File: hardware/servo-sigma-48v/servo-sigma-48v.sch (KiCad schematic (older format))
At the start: 0 parts

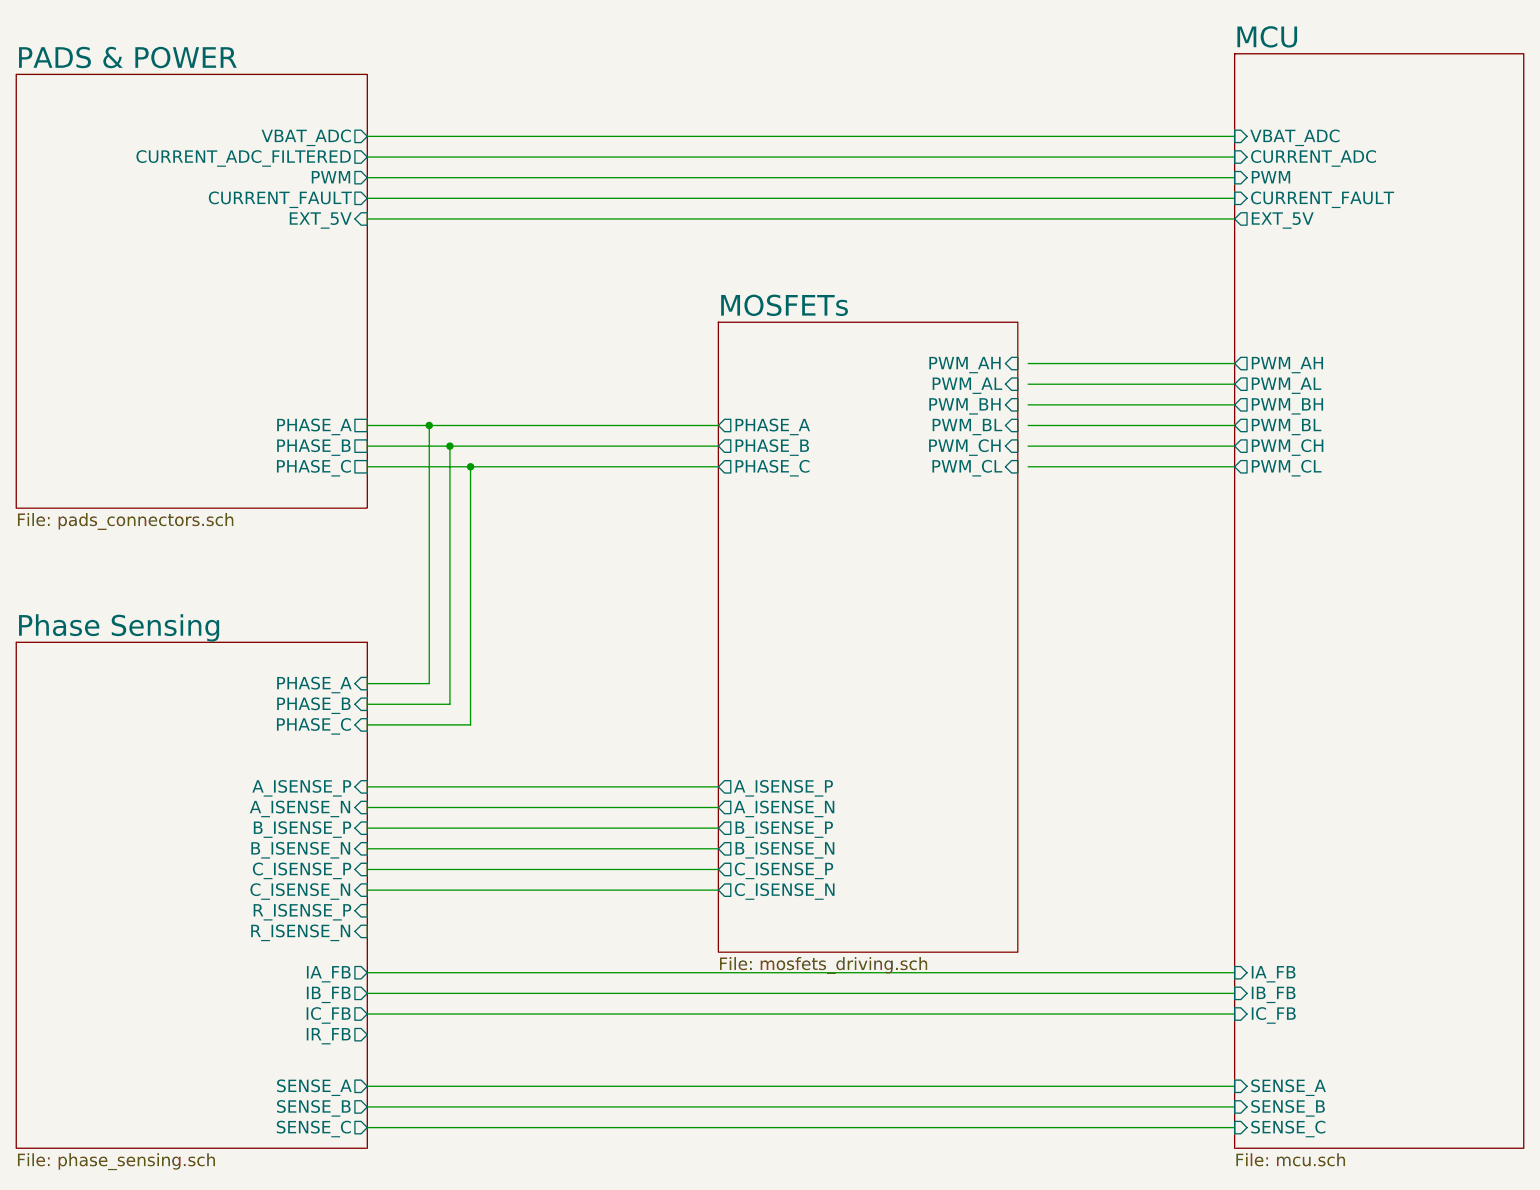
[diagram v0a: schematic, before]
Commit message: Finished routing of the servo controller
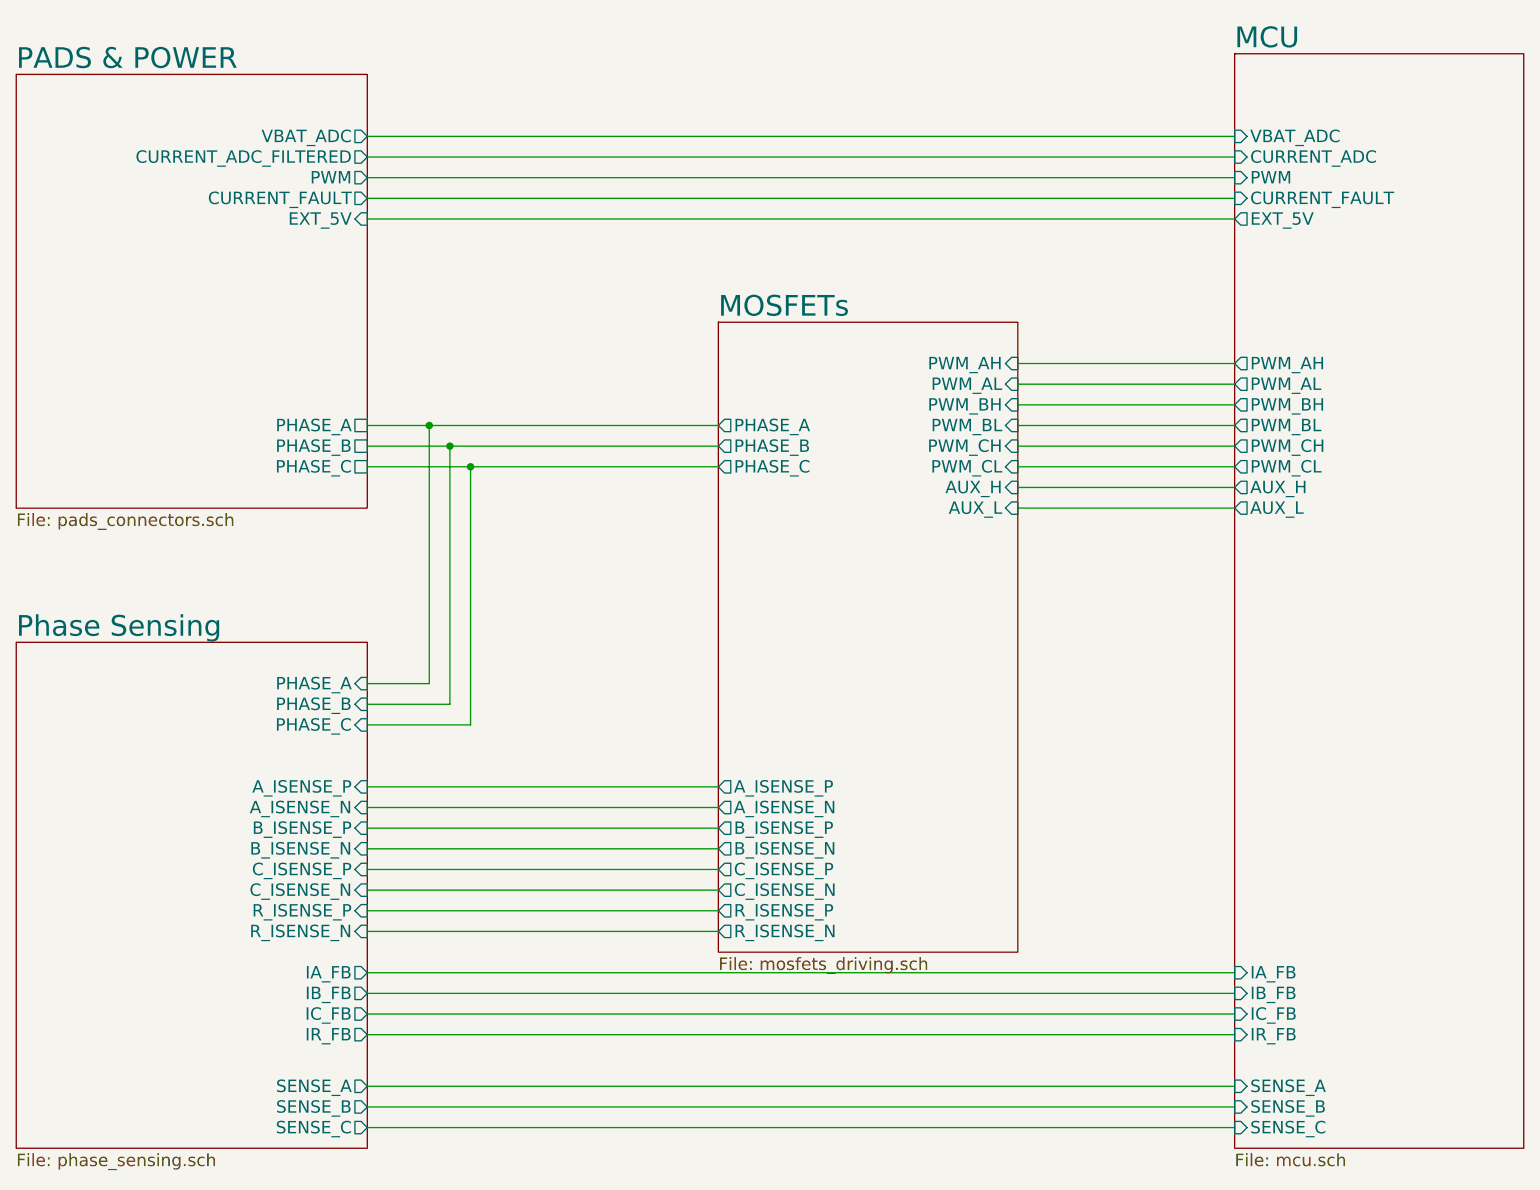
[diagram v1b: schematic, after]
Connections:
- wire segments 35 -> 40
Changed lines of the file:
@@
 F15 "C_ISENSE_P" O L 5200 4750 60
 F16 "C_ISENSE_N" O L 5200 4850 60
+F17 "AUX_L" I R 6650 3000 60
+F18 "AUX_H" I R 6650 2900 60
+F19 "R_ISENSE_P" O L 5200 4950 60
+F20 "R_ISENSE_N" O L 5200 5050 60
 $EndSheet
 $Sheet
@@
 F17 "IB_FB" I L 7700 5350 60
 F18 "IC_FB" I L 7700 5450 60
+F19 "AUX_L" O L 7700 3000 60
+F20 "AUX_H" O L 7700 2900 60
+F21 "IR_FB" I L 7700 5550 60
 $EndSheet
 Wire Wire Line
@@
 	3500 6000 7700 6000
 Wire Wire Line
-	6700 2300 7700 2300
+	6650 2300 7700 2300
 Wire Wire Line
-	6700 2400 7700 2400
+	6650 2400 7700 2400
 Wire Wire Line
-	6700 2500 7700 2500
+	6650 2500 7700 2500
 Wire Wire Line
-	6700 2600 7700 2600
+	6650 2600 7700 2600
 Wire Wire Line
-	6700 2700 7700 2700
+	6650 2700 7700 2700
 Wire Wire Line
-	6700 2800 7700 2800
+	6650 2800 7700 2800
 Wire Wire Line
 	3500 5250 7700 5250
@@
 Wire Wire Line
 	3500 5450 7700 5450
+Wire Wire Line
+	6650 2900 7700 2900
+Wire Wire Line
+	6650 3000 7700 3000
+Wire Wire Line
+	3500 4950 5200 4950
+Wire Wire Line
+	3500 5050 5200 5050
+Wire Wire Line
+	3500 5550 7700 5550
 $EndSCHEMATC

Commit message: Work on sigmadrive 2.0
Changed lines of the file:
@@
 F3 "PHASE_B" U R 3500 2700 60
 F4 "PHASE_C" U R 3500 2800 60
-F5 "CURRENT_ADC_FILTERED" O R 3500 1300 60
-F6 "CURRENT_FAULT" O R 3500 1500 60
-F7 "VBAT_ADC" O R 3500 1200 60
-F8 "PWM" O R 3500 1400 60
-F9 "EXT_5V" I R 3500 1600 60
+F5 "VBAT_ADC" O R 3500 1200 60
+F6 "PWM" O R 3500 1400 60
+F7 "EXT_5V" I R 3500 1600 60
 $EndSheet
 Wire Wire Line
@@
 Wire Wire Line
 	3500 1200 7700 1200
-Wire Wire Line
-	3500 1300 7700 1300
 Wire Wire Line
 	3500 1400 7700 1400
@@
 Connection ~ 4000 2800
 Wire Wire Line
-	3500 1500 7700 1500
-Wire Wire Line
 	3800 2600 5200 2600
 Wire Wire Line
@@
 F4 "SENSE_B" I L 7700 5900 60
 F5 "SENSE_C" I L 7700 6000 60
-F6 "CURRENT_ADC" I L 7700 1300 60
-F7 "PWM_AH" O L 7700 2300 60
-F8 "PWM_AL" O L 7700 2400 60
-F9 "PWM_BH" O L 7700 2500 60
-F10 "PWM_BL" O L 7700 2600 60
-F11 "PWM_CH" O L 7700 2700 60
-F12 "PWM_CL" O L 7700 2800 60
-F13 "PWM" I L 7700 1400 60
-F14 "CURRENT_FAULT" I L 7700 1500 60
-F15 "EXT_5V" O L 7700 1600 60
-F16 "IA_FB" I L 7700 5250 60
-F17 "IB_FB" I L 7700 5350 60
-F18 "IC_FB" I L 7700 5450 60
-F19 "AUX_L" O L 7700 3000 60
-F20 "AUX_H" O L 7700 2900 60
-F21 "IR_FB" I L 7700 5550 60
+F6 "PWM_AH" O L 7700 2300 60
+F7 "PWM_AL" O L 7700 2400 60
+F8 "PWM_BH" O L 7700 2500 60
+F9 "PWM_BL" O L 7700 2600 60
+F10 "PWM_CH" O L 7700 2700 60
+F11 "PWM_CL" O L 7700 2800 60
+F12 "PWM" I L 7700 1400 60
+F13 "EXT_5V" O L 7700 1600 60
+F14 "IA_FB" I L 7700 5250 60
+F15 "IB_FB" I L 7700 5350 60
+F16 "IC_FB" I L 7700 5450 60
+F17 "AUX_L" O L 7700 3000 60
+F18 "AUX_H" O L 7700 2900 60
+F19 "IR_FB" I L 7700 5550 60
 $EndSheet
 Wire Wire Line

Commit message: completed routing
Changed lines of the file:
@@
 $Descr A4 11693 8268
 encoding utf-8
-Sheet 1 5
+Sheet 1 4
 Title "Servo Driver 48V"
 Date "2018-09-03"
@@
 F6 "SENSE_B" O R 3500 5900 60
 F7 "SENSE_A" O R 3500 5800 60
-F8 "A_ISENSE_P" I R 3500 4350 60
-F9 "A_ISENSE_N" I R 3500 4450 60
-F10 "IA_FB" O R 3500 5250 60
-F11 "B_ISENSE_P" I R 3500 4550 60
-F12 "B_ISENSE_N" I R 3500 4650 60
-F13 "IB_FB" O R 3500 5350 60
-F14 "C_ISENSE_P" I R 3500 4750 60
-F15 "C_ISENSE_N" I R 3500 4850 60
-F16 "IC_FB" O R 3500 5450 60
-F17 "IR_FB" O R 3500 5550 60
-F18 "R_ISENSE_P" I R 3500 4950 60
-F19 "R_ISENSE_N" I R 3500 5050 60
 $EndSheet
 $Sheet
@@
 F2 "PWM_AH" I R 6650 2300 60
 F3 "PWM_AL" I R 6650 2400 60
-F4 "PHASE_A" O L 5200 2600 60
+F4 "PHASE_A" O L 5200 3850 60
 F5 "PWM_BH" I R 6650 2500 60
 F6 "PWM_BL" I R 6650 2600 60
-F7 "PHASE_B" O L 5200 2700 60
+F7 "PHASE_B" O L 5200 3950 60
 F8 "PWM_CH" I R 6650 2700 60
 F9 "PWM_CL" I R 6650 2800 60
-F10 "PHASE_C" O L 5200 2800 60
-F11 "A_ISENSE_P" O L 5200 4350 60
-F12 "A_ISENSE_N" O L 5200 4450 60
-F13 "B_ISENSE_P" O L 5200 4550 60
-F14 "B_ISENSE_N" O L 5200 4650 60
-F15 "C_ISENSE_P" O L 5200 4750 60
-F16 "C_ISENSE_N" O L 5200 4850 60
-F17 "AUX_L" I R 6650 3000 60
-F18 "AUX_H" I R 6650 2900 60
-F19 "R_ISENSE_P" O L 5200 4950 60
-F20 "R_ISENSE_N" O L 5200 5050 60
+F10 "PHASE_C" O L 5200 4050 60
+F11 "GATE_ENABLE" I R 6650 3200 60
+F12 "DRV_SDI" I R 6650 3300 60
+F13 "DRV_SDO" O R 6650 3400 60
+F14 "DRV_CLK" I R 6650 3500 60
+F15 "DRV1_CS" I R 6650 3600 60
+F16 "DRV_CAL" I R 6650 3800 60
+F17 "DRV_FAULT" O R 6650 3900 60
+F18 "DRV_SOC" O R 6650 4100 60
+F19 "DRV_SOB" O R 6650 4200 60
+F20 "DRV_SOA" O R 6650 4300 60
+F21 "EXT_5V" I R 6650 4550 60
+F22 "VBAT_ADC" O R 6650 4450 60
+F23 "DRV2_CS" I R 6650 3700 60
+F24 "PWM_RH" I R 6650 2900 60
+F25 "PWM_RL" I R 6650 3000 60
 $EndSheet
-$Sheet
-S 1800 900  1700 2100
-U 58BE27E6
-F0 "PADS & POWER" 100
-F1 "pads_connectors.sch" 60
-F2 "PHASE_A" U R 3500 2600 60
-F3 "PHASE_B" U R 3500 2700 60
-F4 "PHASE_C" U R 3500 2800 60
-F5 "VBAT_ADC" O R 3500 1200 60
-F6 "PWM" O R 3500 1400 60
-F7 "EXT_5V" I R 3500 1600 60
-$EndSheet
-Wire Wire Line
-	3500 2600 3800 2600
-Wire Wire Line
-	3500 2700 3900 2700
-Wire Wire Line
-	3500 2800 4000 2800
-Wire Wire Line
-	3500 1200 7700 1200
-Wire Wire Line
-	3500 1400 7700 1400
-Wire Wire Line
-	3500 3850 3800 3850
-Wire Wire Line
-	3800 3850 3800 2600
-Connection ~ 3800 2600
-Wire Wire Line
-	3500 3950 3900 3950
-Wire Wire Line
-	3900 3950 3900 2700
-Connection ~ 3900 2700
-Wire Wire Line
-	3500 4050 4000 4050
-Wire Wire Line
-	4000 4050 4000 2800
-Connection ~ 4000 2800
-Wire Wire Line
-	3800 2600 5200 2600
-Wire Wire Line
-	3900 2700 5200 2700
-Wire Wire Line
-	4000 2800 5200 2800
 $Sheet
 S 7700 800  1400 5300
@@
 F0 "MCU" 100
 F1 "mcu.sch" 60
-F2 "VBAT_ADC" I L 7700 1200 60
-F3 "SENSE_A" I L 7700 5800 60
-F4 "SENSE_B" I L 7700 5900 60
-F5 "SENSE_C" I L 7700 6000 60
-F6 "PWM_AH" O L 7700 2300 60
-F7 "PWM_AL" O L 7700 2400 60
-F8 "PWM_BH" O L 7700 2500 60
-F9 "PWM_BL" O L 7700 2600 60
-F10 "PWM_CH" O L 7700 2700 60
-F11 "PWM_CL" O L 7700 2800 60
-F12 "PWM" I L 7700 1400 60
-F13 "EXT_5V" O L 7700 1600 60
-F14 "IA_FB" I L 7700 5250 60
-F15 "IB_FB" I L 7700 5350 60
-F16 "IC_FB" I L 7700 5450 60
-F17 "AUX_L" O L 7700 3000 60
-F18 "AUX_H" O L 7700 2900 60
-F19 "IR_FB" I L 7700 5550 60
+F2 "SENSE_A" I L 7700 5800 60
+F3 "SENSE_B" I L 7700 5900 60
+F4 "SENSE_C" I L 7700 6000 60
+F5 "PWM_AH" O L 7700 2300 60
+F6 "PWM_AL" O L 7700 2400 60
+F7 "PWM_BH" O L 7700 2500 60
+F8 "PWM_BL" O L 7700 2600 60
+F9 "PWM_CH" O L 7700 2700 60
+F10 "PWM_CL" O L 7700 2800 60
+F11 "IA_FB" I L 7700 4300 60
+F12 "IB_FB" I L 7700 4200 60
+F13 "IC_FB" I L 7700 4100 60
+F14 "AUX_L" O L 7700 3000 60
+F15 "AUX_H" O L 7700 2900 60
+F16 "EXT_5V" O L 7700 4550 60
+F17 "VBAT_ADC" I L 7700 4450 60
+F18 "DRV_SDI" O L 7700 3300 60
+F19 "DRV_SDO" I L 7700 3400 60
+F20 "DRV_CLK" O L 7700 3500 60
+F21 "DRV1_CS" O L 7700 3600 60
+F22 "DRV_CAL" O L 7700 3800 60
+F23 "DRV_FAULT" I L 7700 3900 60
+F24 "GATE_ENABLE" O L 7700 3200 60
+F25 "DRV2_CS" O L 7700 3700 60
 $EndSheet
-Wire Wire Line
-	3500 1600 7700 1600
-Wire Wire Line
-	3500 4350 5200 4350
-Wire Wire Line
-	3500 4450 5200 4450
-Wire Wire Line
-	3500 4550 5200 4550
-Wire Wire Line
-	3500 4650 5200 4650
-Wire Wire Line
-	3500 4750 5200 4750
-Wire Wire Line
-	3500 4850 5200 4850
 Wire Wire Line
 	3500 5800 7700 5800
@@
 	6650 2800 7700 2800
 Wire Wire Line
-	3500 5250 7700 5250
-Wire Wire Line
-	3500 5350 7700 5350
-Wire Wire Line
-	3500 5450 7700 5450
-Wire Wire Line
 	6650 2900 7700 2900
 Wire Wire Line
 	6650 3000 7700 3000
 Wire Wire Line
-	3500 4950 5200 4950
+	3500 3850 5200 3850
 Wire Wire Line
-	3500 5050 5200 5050
+	3500 3950 5200 3950
 Wire Wire Line
-	3500 5550 7700 5550
+	3500 4050 5200 4050
+Wire Wire Line
+	6650 4100 7700 4100
+Wire Wire Line
+	6650 4200 7700 4200
+Wire Wire Line
+	6650 4300 7700 4300
+Wire Wire Line
+	6650 4450 7700 4450
+Wire Wire Line
+	6650 4550 7700 4550
+Wire Wire Line
+	6650 3200 7700 3200
+Wire Wire Line
+	6650 3300 7700 3300
+Wire Wire Line
+	6650 3400 7700 3400
+Wire Wire Line
+	6650 3500 7700 3500
+Wire Wire Line
+	6650 3600 7700 3600
+Wire Wire Line
+	6650 3800 7700 3800
+Wire Wire Line
+	6650 3900 7700 3900
+Wire Wire Line
+	6650 3700 7700 3700
 $EndSCHEMATC
